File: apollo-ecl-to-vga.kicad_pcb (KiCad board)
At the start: 2 copper layers, 55 x 36.2 mm, 15 parts, among them IC1 SY100ELT25ZG-TR, J1 DB9_Female, J2 DB15_Female

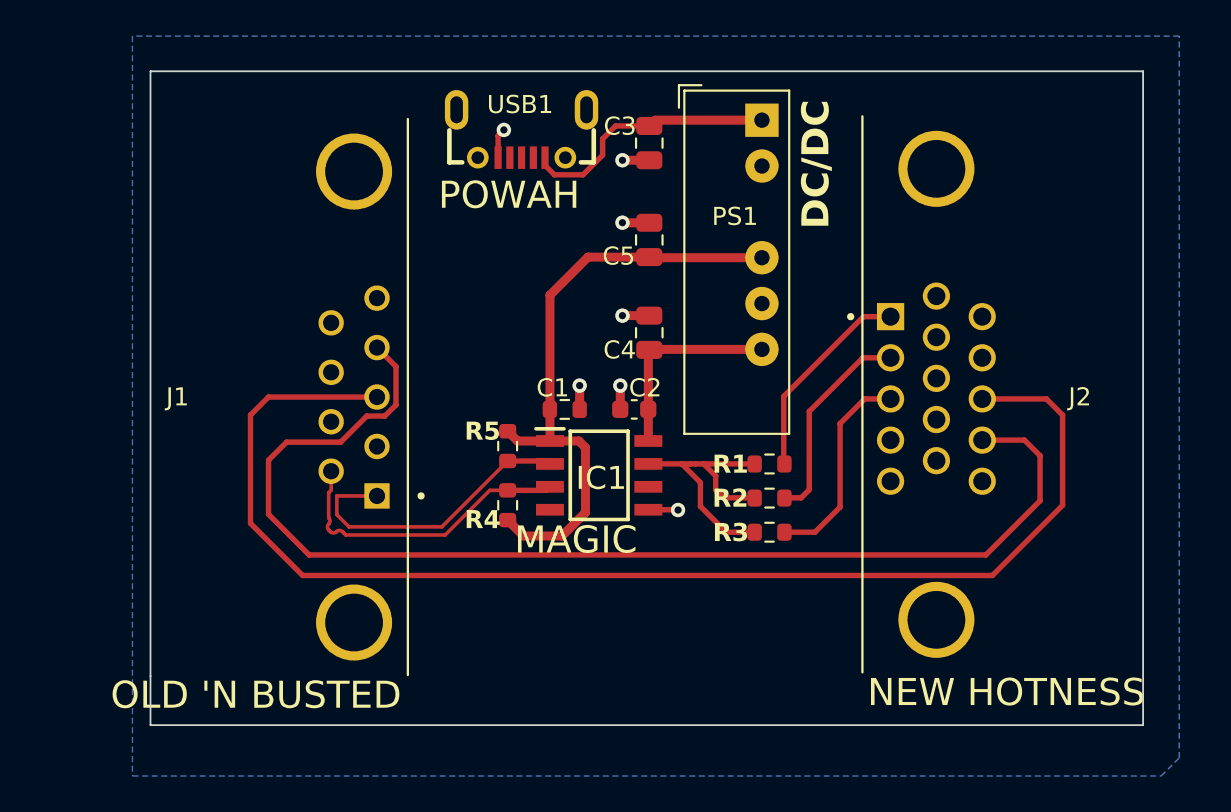
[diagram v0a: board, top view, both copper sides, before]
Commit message: switch from 0805 to 0603 since they're being assembled anyway
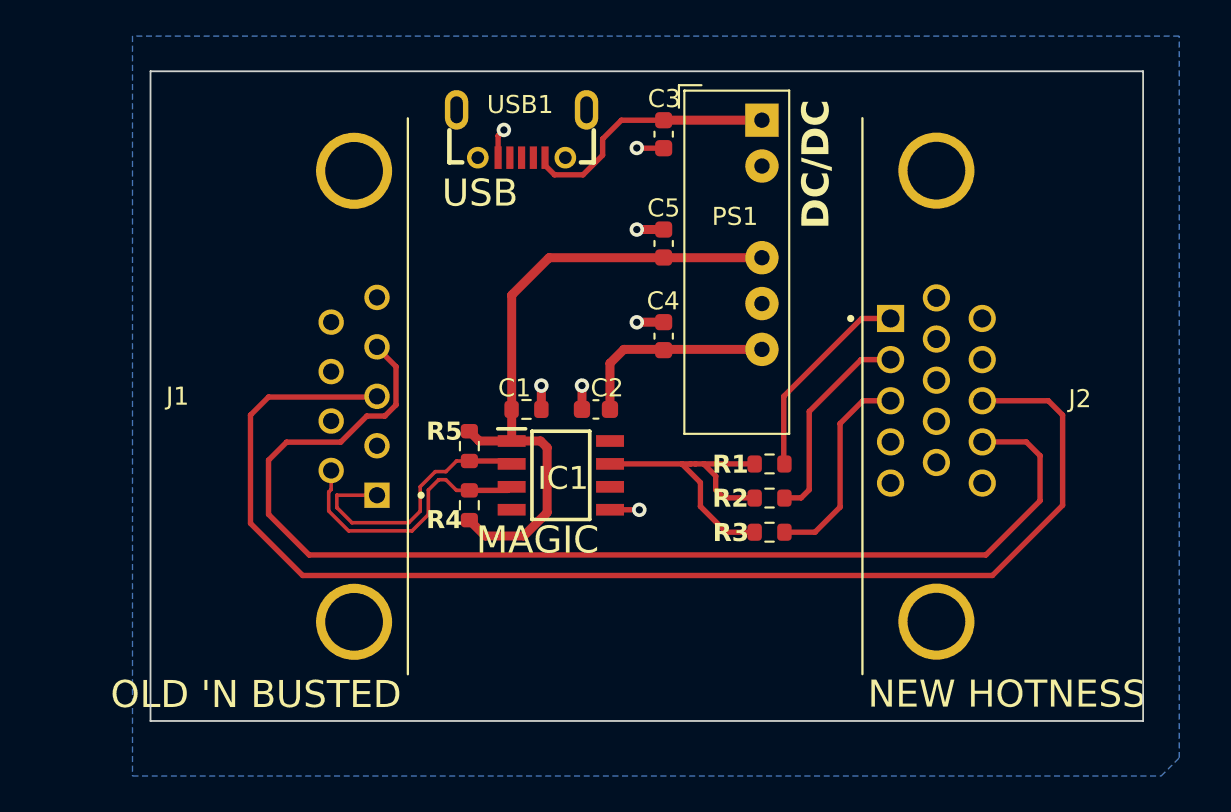
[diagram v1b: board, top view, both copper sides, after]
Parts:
- C3, C4, C5: footprint Capacitor_SMD:C_0805_2012Metric -> Capacitor_SMD:C_0603_1608Metric
- moved C1 2.12 mm to (87.8, 89.7)
- moved C2 2.12 mm to (91.7, 89.7)
- moved IC1 2.12 mm to (89.7, 93.3)
- moved R4 2.12 mm to (84.7, 95.0)
- moved R5 2.12 mm to (84.7, 91.7)
- moved C3 0.94 mm to (95.4, 74.4)
- moved C5 0.82 mm to (95.4, 80.5)
- moved C4 0.82 mm to (95.4, 85.6)
- moved J2 0.10 mm to (110.5, 89.0)
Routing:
- net -5V: track 34.2 -> 36.4 mm
- net /video_out: track 16.2 -> 18.3 mm
- net /video-: track 16.9 -> 15.2 mm
- net /video+: track 16.9 -> 15.2 mm
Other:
- board size 55 x 36.2 mm -> 55 x 36 mm
